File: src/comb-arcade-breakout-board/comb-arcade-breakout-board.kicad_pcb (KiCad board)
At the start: 2 copper layers, 114.5 x 13.7 mm, 9 parts, among them J1 Game_Connector, J2 PWR_DANGEROUS, J3 PWR_SAFE, J4 COIN_SLOTS, J5 SPEAKER, J6 VIDEO, J7 MISC_INPUTS, J8 P1, J9 P2

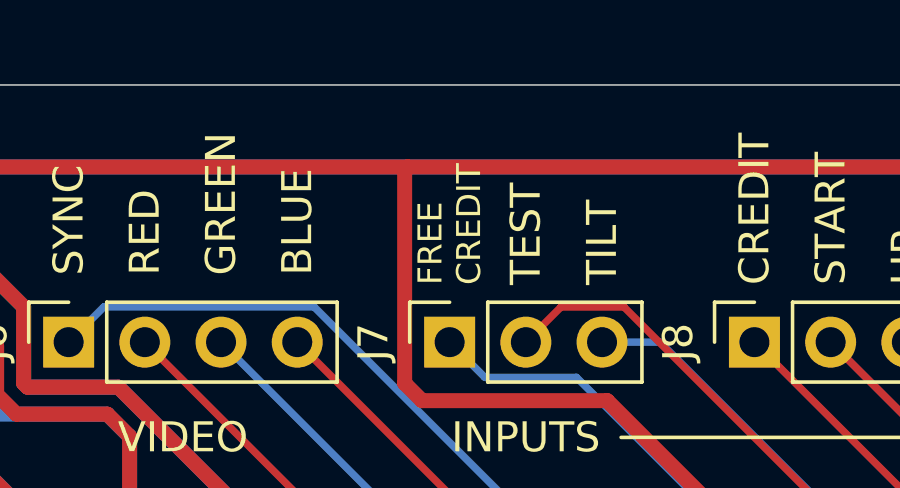
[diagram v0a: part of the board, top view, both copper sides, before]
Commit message: Rename FREE CREDIT to SERVICE.
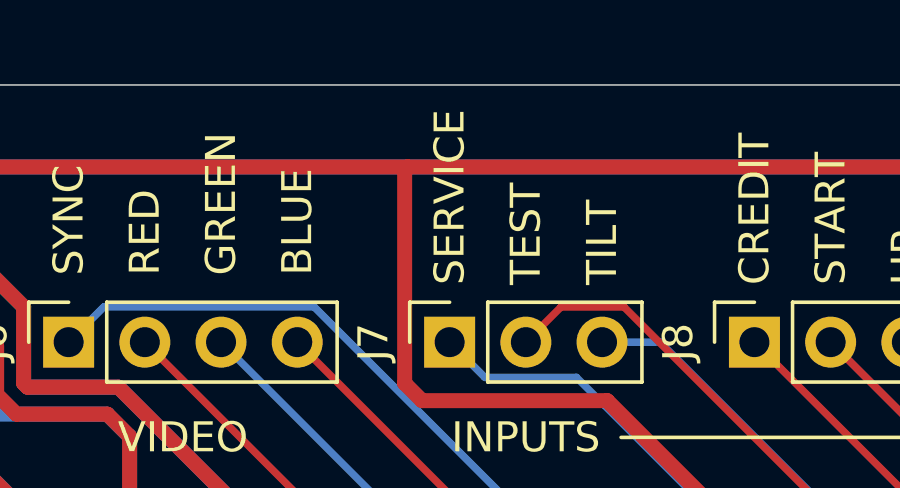
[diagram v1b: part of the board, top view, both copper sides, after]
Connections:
- net FREE_CREDIT renamed SERVICE
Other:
- board text added: "SERVICE"
- board text removed: "FREE CREDIT"

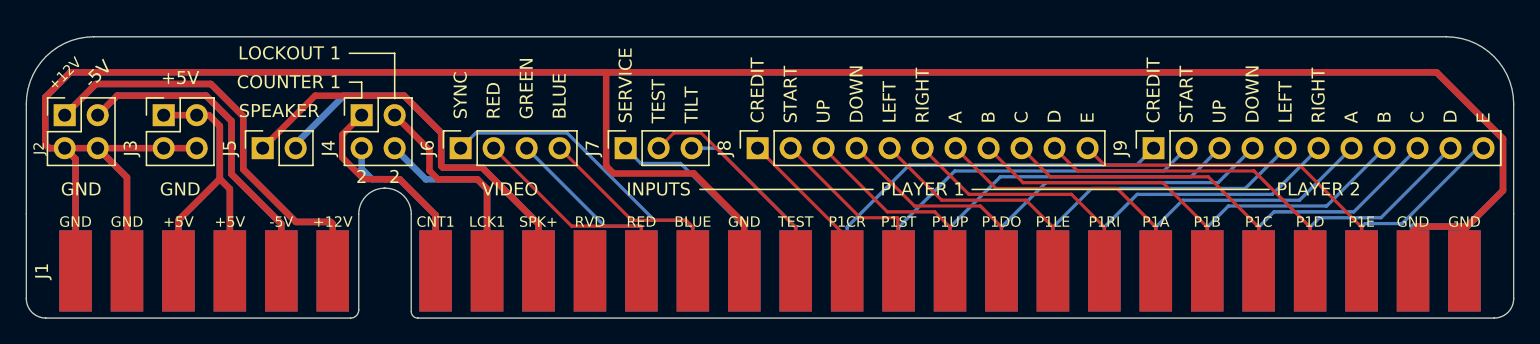
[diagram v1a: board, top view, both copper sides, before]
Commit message: Fix DRC.
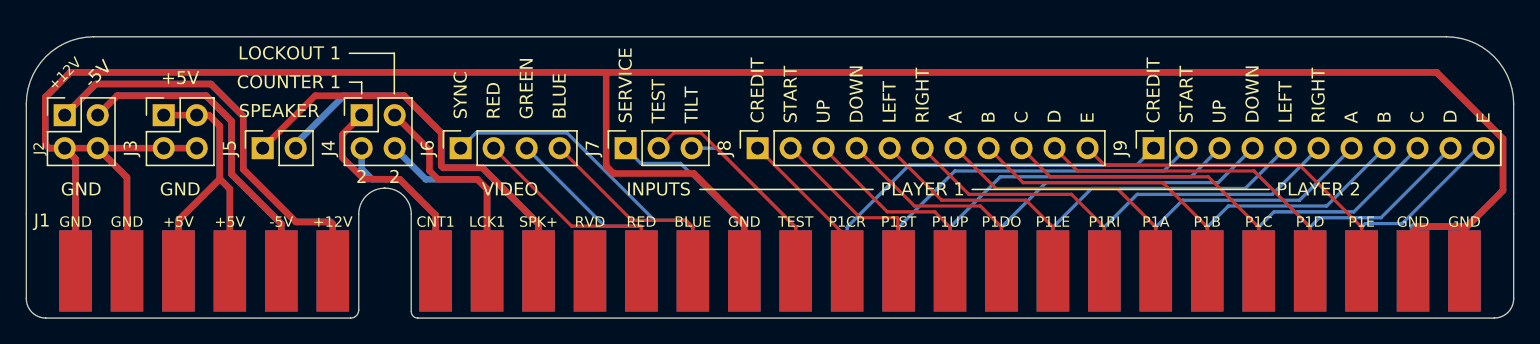
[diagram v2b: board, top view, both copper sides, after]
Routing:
- net P2_E: track 16.3 -> 15.3 mm
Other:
- net class Default removed
- net class Power removed
